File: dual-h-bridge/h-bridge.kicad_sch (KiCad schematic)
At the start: 13 parts, among them Q10 VN2222L, Q3 IRFZ44, Q4 IRFZ44, Q5 2N3904, Q6 VN2222L, Q7 IRFZ44, Q8 IRFZ44, Q9 2N3904

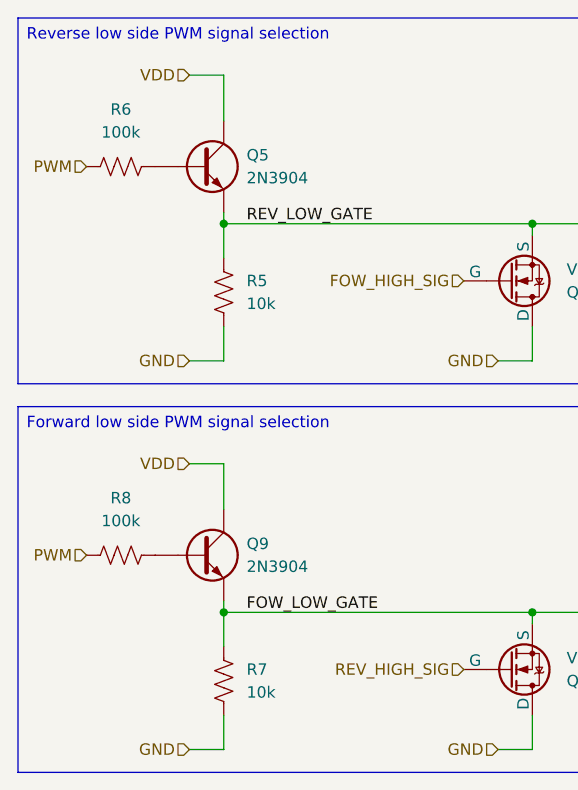
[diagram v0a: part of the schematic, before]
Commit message: Fix potentially inverted H-Bridge direction bit
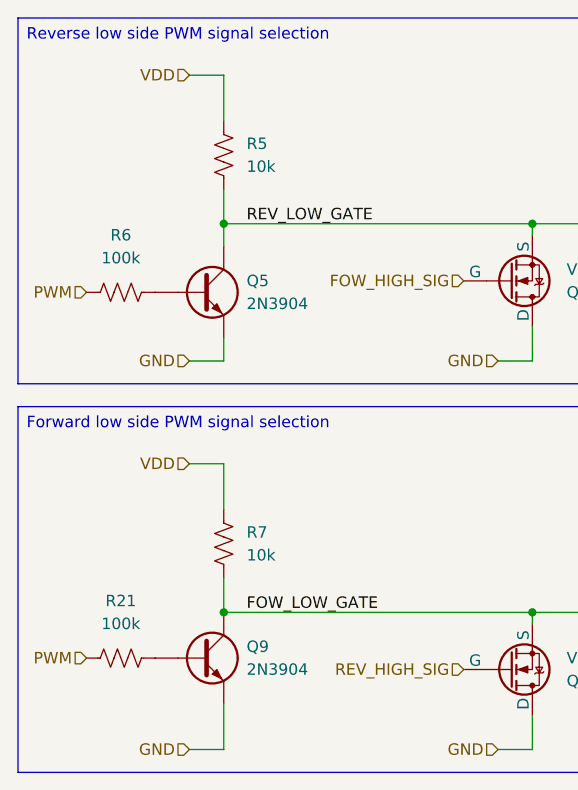
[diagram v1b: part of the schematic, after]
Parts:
- removed R8: 100k, Resistor_THT:R_Axial_DIN0309_L9.0mm_D3.2mm_P12.70mm_Horizontal, symbol GS_Resistor_THT:R_250mW
- added R21: 100k, Resistor_THT:R_Axial_DIN0309_L9.0mm_D3.2mm_P12.70mm_Horizontal, symbol GS_Resistor_THT:R_250mW
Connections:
- net FOW_LOW_GATE: now also Q9.3 (C), R7.2; no longer Q9.1 (E), R7.1
- net GND: now also Q5.1 (E), Q9.1 (E); no longer R5.2, R7.2
- net PWM: now also R21.1
- net REV_LOW_GATE: now also Q5.3 (C), R5.2; no longer Q5.1 (E), R5.1
- net VDD: now also R5.1, R7.1; no longer Q5.3 (C), Q9.3 (C)
- net at Q9.2 (B): now also R21.2
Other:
- moved on the sheet: Q5, Q9, R5, R6, R7

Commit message: Some small updates
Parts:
- R21, R6: value 100k -> 10k
- R5, R7: value 10k -> 1k
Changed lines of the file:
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@@
 		(title "H-Bridge")
 		(date "2025-07-09")
-		(rev "v3.0.0")
+		(rev "v4.0.0")
 		(company "Team 5")
 		(comment 1 "George Sleen")
@@
 			)
 		)
-		(property "Value" "100k"
+		(property "Value" "10k"
 			(at 27.94 43.18 90)
 			(effects
@@
 			)
 		)
-		(property "Value" "100k"
+		(property "Value" "10k"
 			(at 27.94 83.82 90)
 			(effects
@@
 			)
 		)
-		(property "Value" "10k"
+		(property "Value" "1k"
 			(at 41.91 33.0199 0)
 			(effects
@@
 			)
 		)
-		(property "Value" "10k"
+		(property "Value" "1k"
 			(at 41.91 76.1999 0)
 			(effects

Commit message: More changes
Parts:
- R21, R6: value 10k -> 100k
- R5, R7: value 1k -> 10k
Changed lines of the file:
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@@
 			)
 		)
-		(property "Value" "10k"
+		(property "Value" "100k"
 			(at 27.94 43.18 90)
 			(effects
@@
 			)
 		)
-		(property "Value" "10k"
+		(property "Value" "100k"
 			(at 27.94 83.82 90)
 			(effects
@@
 			)
 		)
-		(property "Value" "1k"
+		(property "Value" "10k"
 			(at 41.91 33.0199 0)
 			(effects
@@
 			)
 		)
-		(property "Value" "1k"
+		(property "Value" "10k"
 			(at 41.91 76.1999 0)
 			(effects

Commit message: Fix all hardware issues and generate final release source files
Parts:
- C13: symbol GS_Capacitor_THT:C_THT_100nF -> GS_Capacitor_THT:C_THT_Ceramic_Disk
- renumbered Q6 to Q5, Q5 to Q6, R21 to R8
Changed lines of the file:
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@@
 		(dnp no)
 		(fields_autoplaced yes)
-		(property "Reference" "Q5"
+		(property "Reference" "Q6"
 			(at 41.91 45.7199 0)
 			(effects
@@
 			(project "motor-controller"
 				(path "/3cf627b4-179f-4b19-ad57-a5207e12b14c/4e94ea2c-a108-4be2-8ee4-b6e71c617b37"
-					(reference "Q13")
-					(unit 1)
-				)
-				(path "/3cf627b4-179f-4b19-ad57-a5207e12b14c/8bf0a1e8-4227-49ee-854f-9e27e5e507a9"
-					(reference "Q5")
+					(reference "Q14")
+					(unit 1)
+				)
+				(path "/3cf627b4-179f-4b19-ad57-a5207e12b14c/8bf0a1e8-4227-49ee-854f-9e27e5e507a9"
+					(reference "Q6")
 					(unit 1)
 				)
@@
 	)
 	(symbol
-		(lib_id "GS_Capacitor_THT:C_THT_100nF")
+		(lib_id "GS_Capacitor_THT:C_THT_Ceramic_Disk")
 		(at 151.13 41.91 90)
 		(mirror x)
@@
 			)
 		)
-		(property "Description" "100nF Unpolarized Capacitor"
+		(property "Description" "Unpolarized Capacitor"
 			(at 135.382 41.91 0)
 			(effects
@@
 		(dnp no)
 		(fields_autoplaced yes)
-		(property "Reference" "Q6"
+		(property "Reference" "Q5"
 			(at 77.47 46.9901 0)
 			(effects
@@
 			(project "motor-controller"
 				(path "/3cf627b4-179f-4b19-ad57-a5207e12b14c/4e94ea2c-a108-4be2-8ee4-b6e71c617b37"
-					(reference "Q14")
-					(unit 1)
-				)
-				(path "/3cf627b4-179f-4b19-ad57-a5207e12b14c/8bf0a1e8-4227-49ee-854f-9e27e5e507a9"
-					(reference "Q6")
+					(reference "Q13")
+					(unit 1)
+				)
+				(path "/3cf627b4-179f-4b19-ad57-a5207e12b14c/8bf0a1e8-4227-49ee-854f-9e27e5e507a9"
+					(reference "Q5")
 					(unit 1)
 				)
@@
 		(dnp no)
 		(fields_autoplaced yes)
-		(property "Reference" "R21"
+		(property "Reference" "R8"
 			(at 27.94 81.28 90)
 			(effects
@@
 			(project "dual-h-bridge"
 				(path "/3cf627b4-179f-4b19-ad57-a5207e12b14c/4e94ea2c-a108-4be2-8ee4-b6e71c617b37"
-					(reference "R22")
-					(unit 1)
-				)
-				(path "/3cf627b4-179f-4b19-ad57-a5207e12b14c/8bf0a1e8-4227-49ee-854f-9e27e5e507a9"
-					(reference "R21")
-					(unit 1)
-				)
+					(reference "R12")
+					(unit 1)
+				)
+				(path "/3cf627b4-179f-4b19-ad57-a5207e12b14c/8bf0a1e8-4227-49ee-854f-9e27e5e507a9"
+					(reference "R8")
+					(unit 1)
+				)

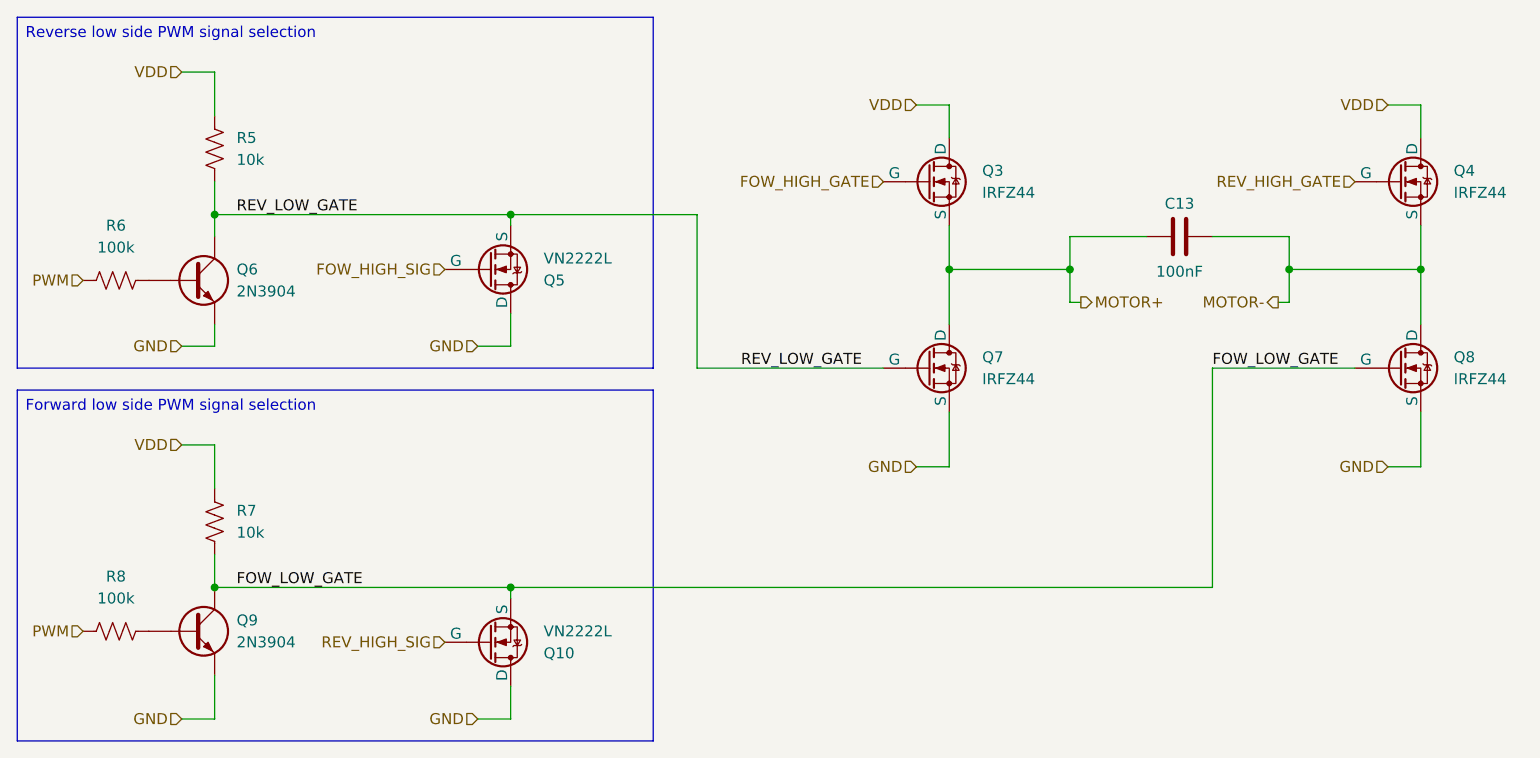
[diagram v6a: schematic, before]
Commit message: Fix source and drain being swapped on small signal mosfet
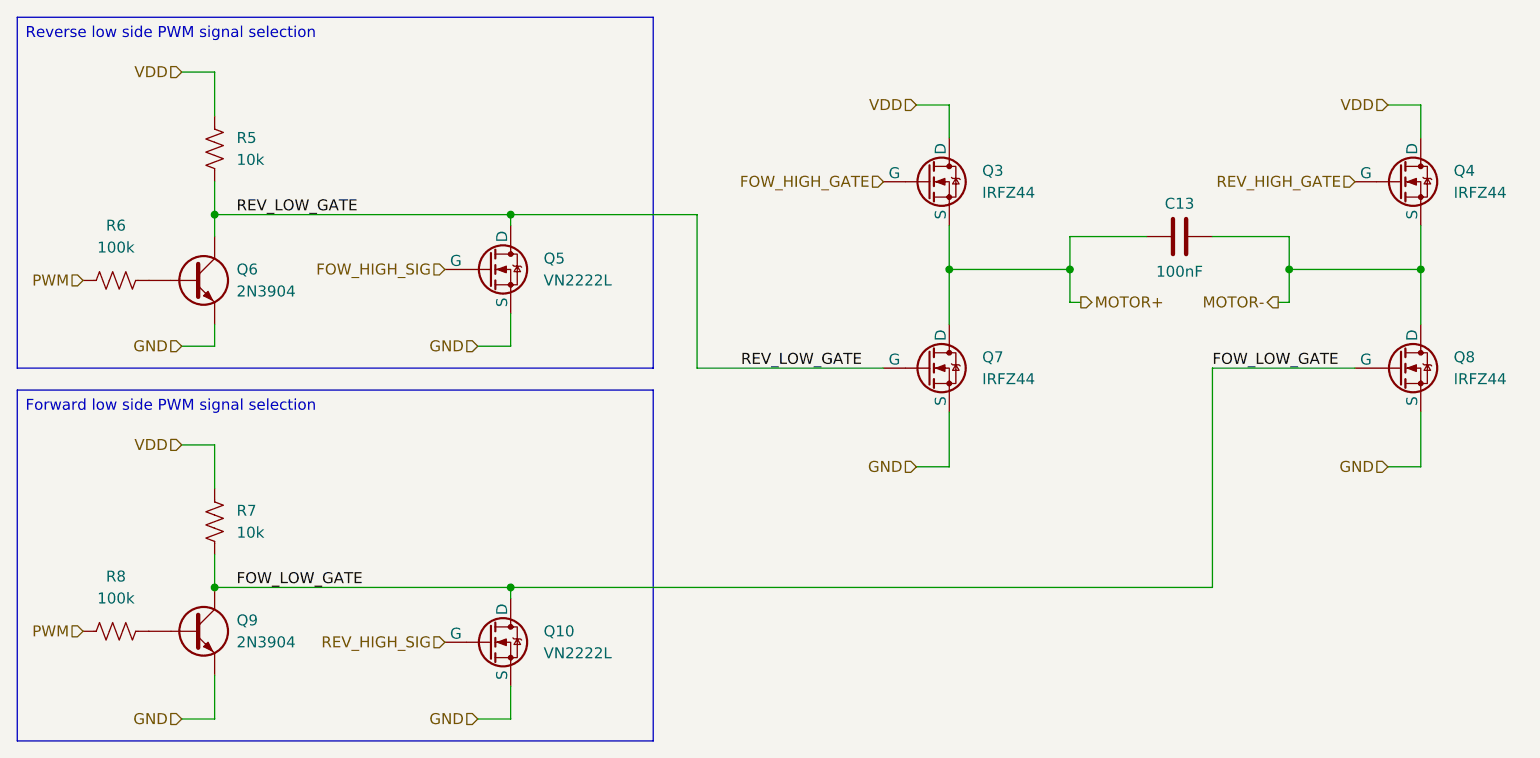
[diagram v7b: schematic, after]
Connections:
- net FOW_LOW_GATE: now also Q10.3 (D); no longer Q10.1 (S)
- net GND: now also Q10.1 (S), Q5.1 (S); no longer Q10.3 (D), Q5.3 (D)
- net REV_LOW_GATE: now also Q5.3 (D); no longer Q5.1 (S)
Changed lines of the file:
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@@
 	(title_block
 		(title "H-Bridge")
-		(date "2025-07-09")
-		(rev "v4.0.0")
+		(date "2025-07-17")
+		(rev "v5.0.0")
 		(company "Team 5")
 		(comment 1 "George Sleen")
@@
 		(lib_id "GS_Transistors:MOSFET_N-Ch_60V_0.23A_7500mR")
 		(at 71.12 45.72 0)
-		(mirror x)
 		(unit 1)
 		(exclude_from_sim no)
@@
 		(on_board yes)
 		(dnp no)
-		(fields_autoplaced yes)
 		(property "Reference" "Q5"
-			(at 77.47 46.9901 0)
+			(at 77.47 44.4499 0)
 			(effects
 				(font
@@
 		)
 		(property "Value" "VN2222L"
-			(at 77.47 44.4501 0)
+			(at 77.47 46.9899 0)
 			(effects
 				(font
@@
 		)
 		(property "Footprint" "Package_TO_SOT_THT:TO-92_Inline"
-			(at 76.2 84.836 0)
+			(at 76.2 6.604 0)
 			(effects
 				(font
@@
 		)
 		(property "Datasheet" "https://ww1.microchip.com/downloads/en/DeviceDoc/VN2222LL%20B082013.pdf"
-			(at 71.12 69.596 0)
+			(at 71.12 21.844 0)
 			(effects
 				(font
@@
 		)
 		(property "Description" "N-MOSFET transistor"
-			(at 71.12 82.296 0)
+			(at 71.12 9.144 0)
 			(effects
 				(font
@@
 		(lib_id "GS_Transistors:MOSFET_N-Ch_60V_0.23A_7500mR")
 		(at 71.12 88.9 0)
-		(mirror x)
 		(unit 1)
 		(exclude_from_sim no)
@@
 		(on_board yes)
 		(dnp no)
-		(fields_autoplaced yes)
 		(property "Reference" "Q10"
-			(at 77.47 90.1701 0)
+			(at 77.47 87.6299 0)
 			(effects
 				(font
@@
 		)
 		(property "Value" "VN2222L"
-			(at 77.47 87.6301 0)
+			(at 77.47 90.1699 0)
 			(effects
 				(font
@@
 		)
 		(property "Footprint" "Package_TO_SOT_THT:TO-92_Inline"
-			(at 76.2 128.016 0)
+			(at 76.2 49.784 0)
 			(effects
 				(font
@@
 		)
 		(property "Datasheet" "https://ww1.microchip.com/downloads/en/DeviceDoc/VN2222LL%20B082013.pdf"
-			(at 71.12 112.776 0)
+			(at 71.12 65.024 0)
 			(effects
 				(font
@@
 		)
 		(property "Description" "N-MOSFET transistor"
-			(at 71.12 125.476 0)
-			(effects
-				(font
+			(at 71.12 52.324 0)
+			(effects
+				(font
